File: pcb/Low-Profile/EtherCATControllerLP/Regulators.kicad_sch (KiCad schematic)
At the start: 0 parts

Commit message: checkpoint
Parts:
- added C12, C13, C39: 2.2uF, symbol Device:C_Small
- added C14: 0.1uF, symbol Device:C_Small
- added C15: 6800pF, symbol Device:C_Small
- added C16, C17: 4.7uF, Capacitor_SMD:C_0805_2012Metric, symbol Device:C
- added C18: 39pF, symbol Device:C_Small
- added C37: 4.7pF, symbol Device:C_Small
- added C38, C55, C78: 470nF, symbol Device:C_Small
- added C74, C75: 47uF, symbol Device:C_Small
- added C76: 150uF, symbol Device:C_Small
- added D1: LTST-C190KGKT, Diode_SMD:D_0603_1608Metric, symbol LTST-C190KGKT:LTST-C190KGKT
- added D2: B560C, symbol Device:D_Schottky
- added L1: 8.2uH, symbol Device:L_Small
- added L2: 5.6uH, symbol Device:L_Small
- added R1: 162K, symbol Device:R_Small
- added R2: 523K, symbol Device:R_Small
- added R3: 84.5, symbol Device:R_Small
- added R38: 53.6K, symbol Device:R_Small
- added R39: 10.2K, symbol Device:R_Small
- added R4: 13K, symbol Device:R_Small
- added R40: 100k, symbol Device:R_Small
- added R41: 100K, symbol Device:R_Small
- added R42: 43.2K, symbol Device:R_Small
- added R5: 1k, Resistor_SMD:R_0603_1608Metric, symbol Device:R
- added TP2, TP3, TP5: TESTPOINT, TestPoint:TestPoint_Pad_1.0x1.0mm, symbol Connector:TestPoint
- added U2: TPS54360DDAR, Package_SO:TI_SO-PowerPAD-8_ThermalVias, symbol Regulator_Switching:TPS54360DDA
- added U3: LDL1117S33R, Package_TO_SOT_SMD:SOT-223, symbol LDL1117S33R:LDL1117S33R
- added U4: LM76005RNPR, symbol 2024-07-02_05-34-37:LM76005RNPR
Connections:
- new net: D1.2, R5.1, TP2.1
- new net: R2.2, R3.1
- new net: C14.1, U2.1 (BOOT)
- new net: R1.1, U2.4 (RT/CLK)
- new net: C18.1, R4.1, U2.6 (COMP)
- new net: C14.2, D2.1 (K), L1.1, U2.8 (SW)
- new net: C15.1, R4.2
- new net: R40.2, U4.16 (PGOOD)
- new net: C55.2, U4.6 (CBOOT)
- new net: C39.2, U4.8 (VCC)
- new net 5V: C74.1, C75.1, L1.2, R38.1, TP3.1, U3.3 (VIN)
- new net DCBUS: C12.1, C13.1, C37.1, C38.1, R2.1, U2.2 (VIN), U4.18 (EN), U4.20 (PVIN), U4.21 (PVIN), U4.22 (PVIN)
- new net EtherCAT3v3: C76.1, C78.1, L2.2, R41.1, TP5.1
- new net FB: R38.2, R39.1, U2.5 (FB)
- new net FB1: R41.2, R42.1, U4.12 (FB)
- new net GND: C12.2, C13.2, C15.2, C16.2, C17.2, C18.2, C37.2, C38.2, C39.1, C74.2, C75.2, C76.2, C78.2, D2.2 (A), R1.2, R3.2, R39.2, R42.2, R5.2, U2.3 (EN), U2.7 (GND), U2.9 (GNDPAD), U3.1 (GND), U4.13 (AGND), U4.14 (AGND), U4.15 (AGND), U4.17 (SYNC_MODE), U4.24 (PGND), U4.25 (PGND), U4.26 (PGND), U4.31 (PAD), U4.9 (BIAS)
- new net PGOOD: C55.1, L2.1, R40.1, U4.1 (SW), U4.2 (SW), U4.3 (SW), U4.4 (SW), U4.5 (SW)
- new net VCC: C16.1, C17.1, D1.1, U3.2 (VOUT), U3.4 (VOUT)
- no-connect marks 0 -> 9
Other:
- note added: "5V out"
- note added: "Digital 3v3"
- note added: "EtherCAT 3v3"

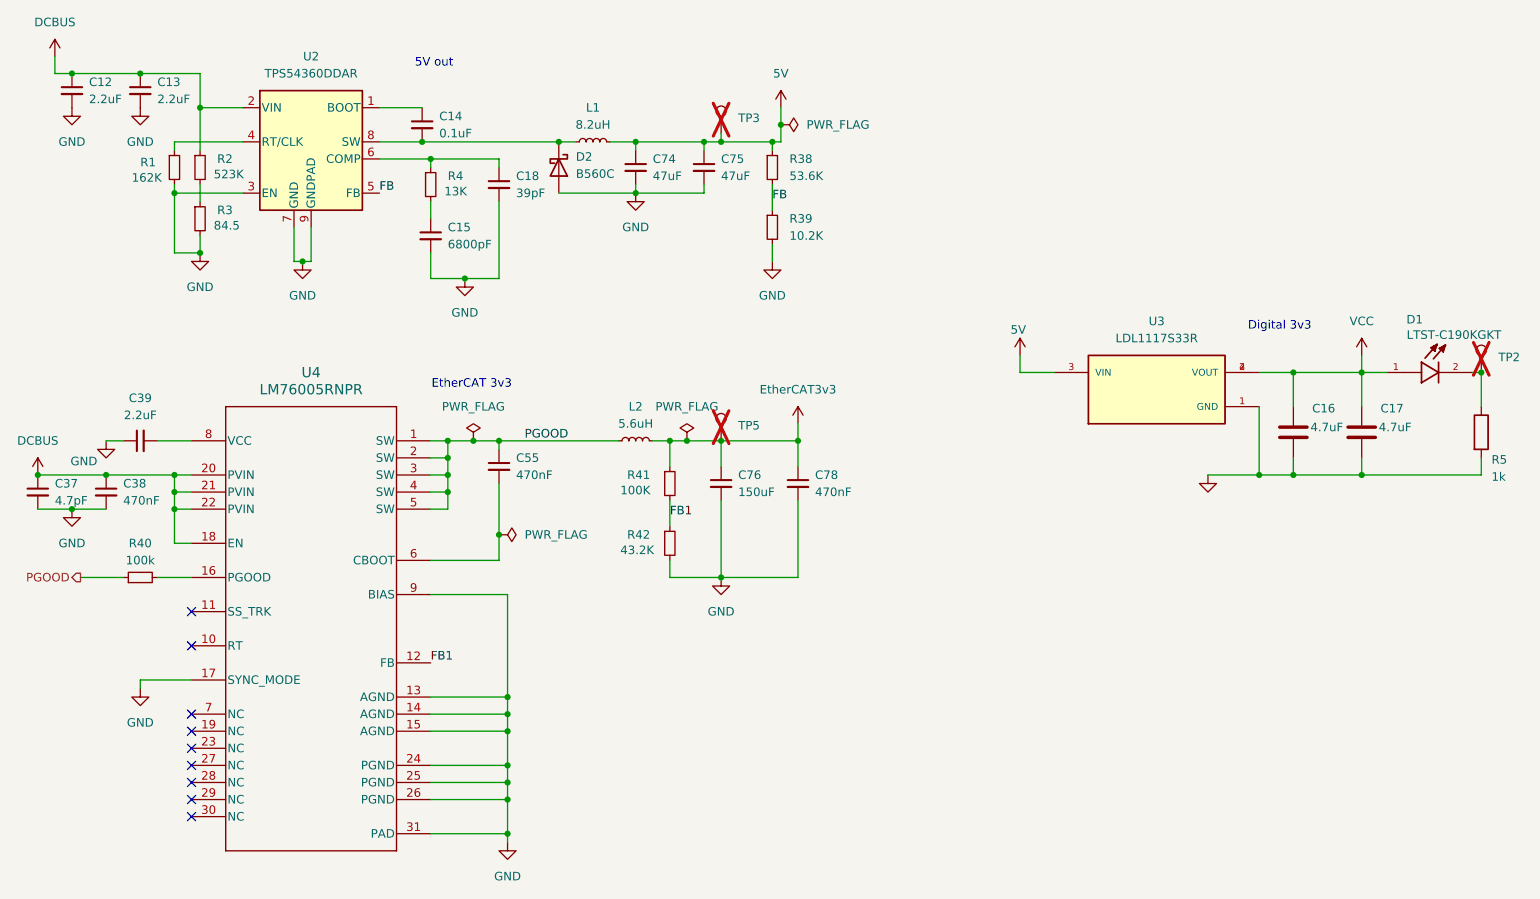
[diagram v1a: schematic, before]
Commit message: Added XMC4800
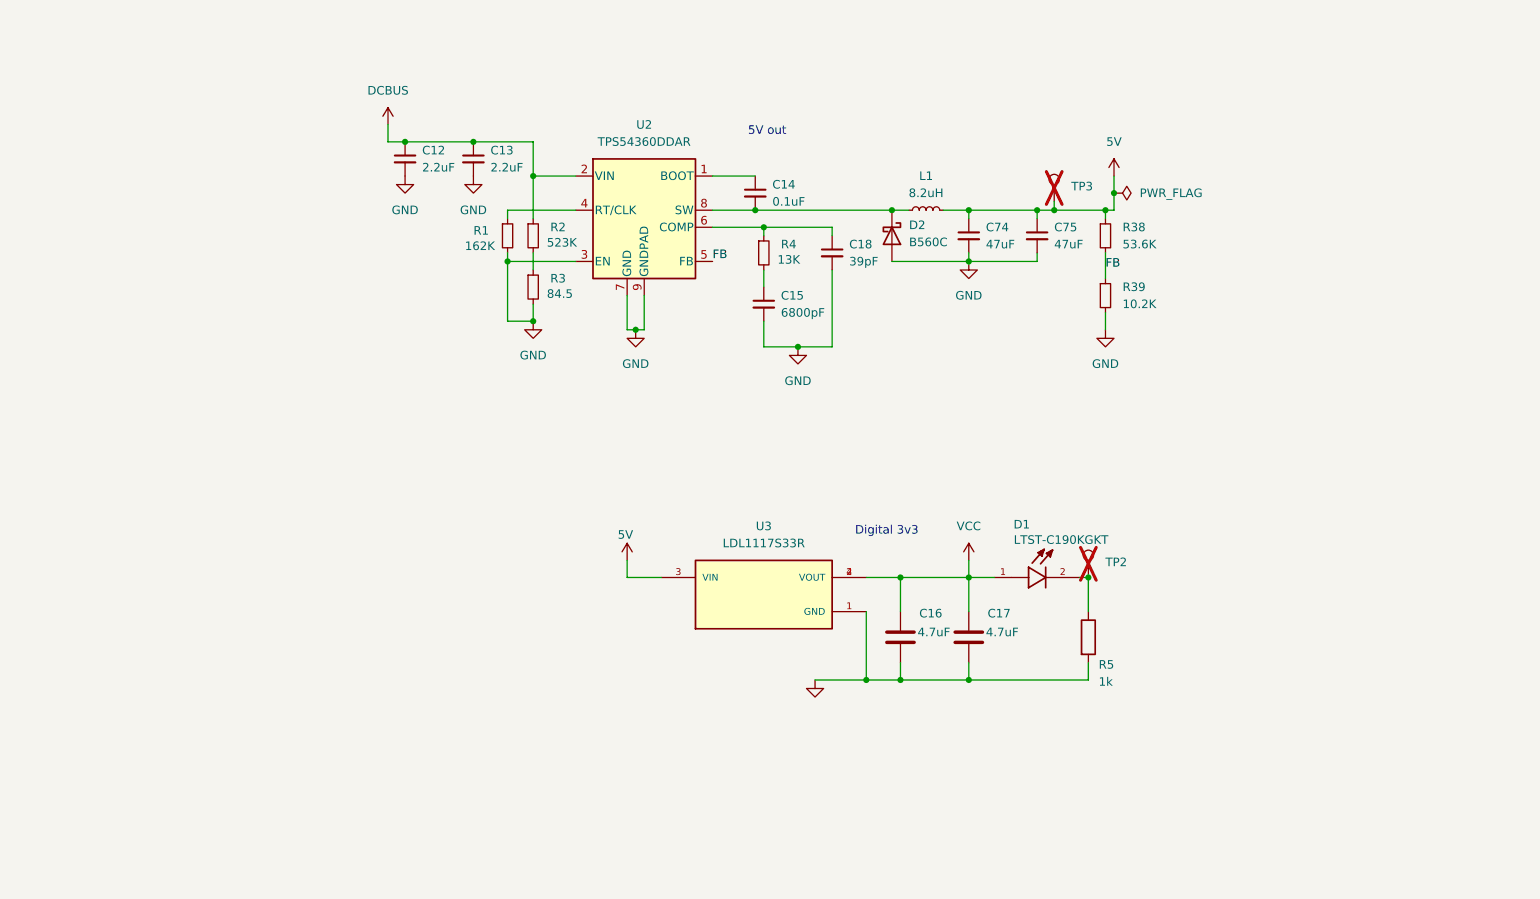
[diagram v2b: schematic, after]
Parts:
- removed C37: 4.7pF, symbol Device:C_Small
- removed C38, C55, C78: 470nF, symbol Device:C_Small
- removed C39: 2.2uF, symbol Device:C_Small
- removed C76: 150uF, symbol Device:C_Small
- removed L2: 5.6uH, symbol Device:L_Small
- removed R40: 100k, symbol Device:R_Small
- removed R41: 100K, symbol Device:R_Small
- removed R42: 43.2K, symbol Device:R_Small
- removed TP5: TESTPOINT, TestPoint:TestPoint_Pad_1.0x1.0mm, symbol Connector:TestPoint
- removed U4: LM76005RNPR, symbol 2024-07-02_05-34-37:LM76005RNPR
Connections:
- no-connect marks 9 -> 0
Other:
- note removed: "EtherCAT 3v3"
- moved on the sheet: C12, C13, C14, C15, C16, C17, C18, C74, C75, D1, D2, L1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
